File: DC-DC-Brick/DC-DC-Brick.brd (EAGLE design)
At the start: 50.8 x 76.2 mm, 20 parts

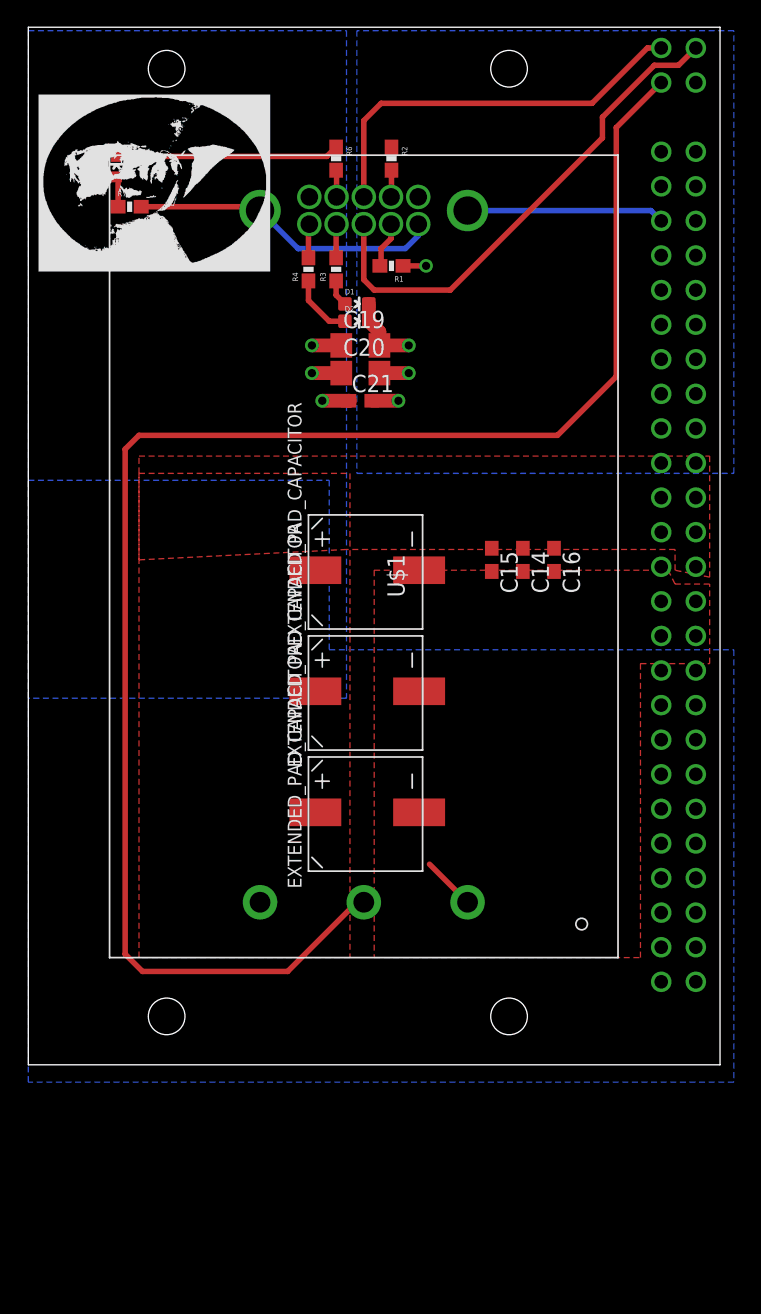
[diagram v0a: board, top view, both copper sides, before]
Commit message: FIxed connection issue
Gnd not connected in J purdue eye LED - fixed
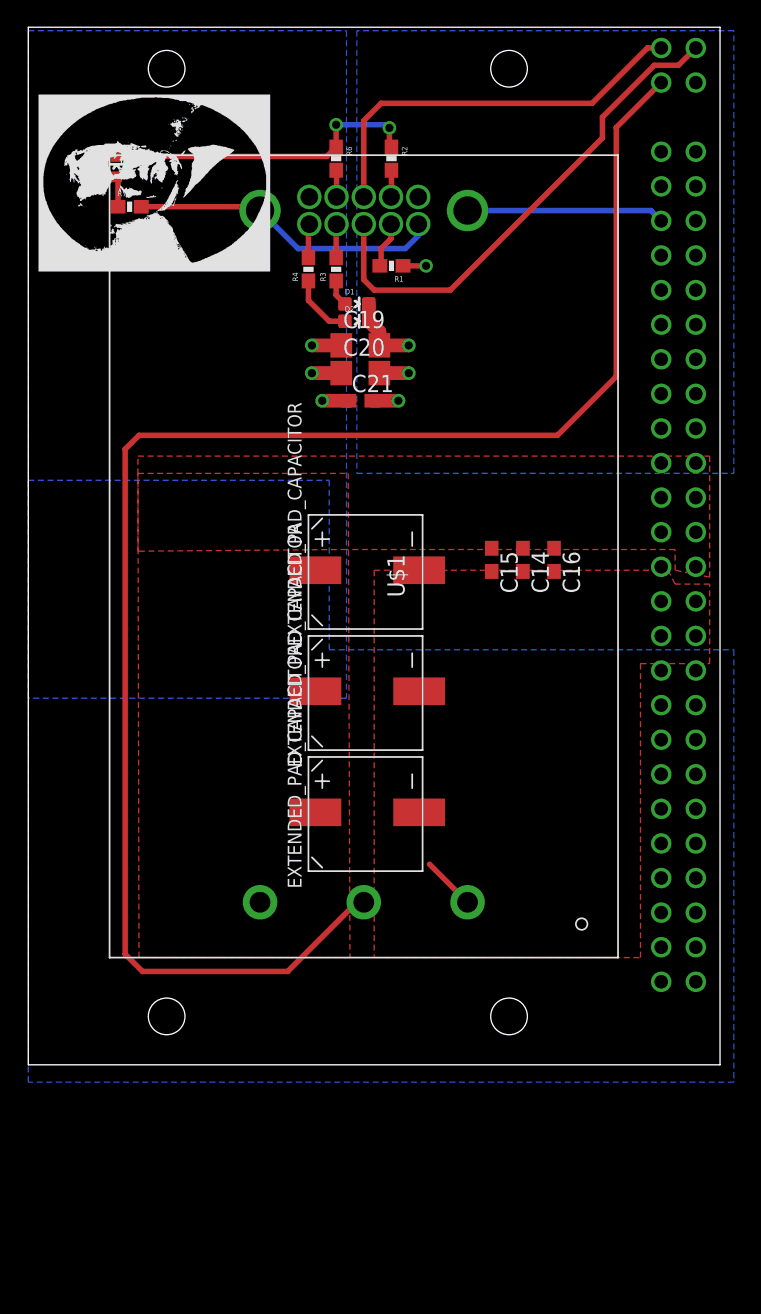
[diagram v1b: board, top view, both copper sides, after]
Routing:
- net GND: track 42.3 -> 49.4 mm, vias 4 -> 6
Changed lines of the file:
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@@
 <wire x1="6.477" y1="66.7138" x2="21.9218" y2="66.7138" width="0.4064" layer="1"/>
 <wire x1="21.9218" y1="66.7138" x2="22.606" y2="67.398" width="0.4064" layer="1"/>
-<wire x1="22.606" y1="67.398" x2="26.67" y2="67.398" width="0" layer="19" extent="1-1"/>
-<wire x1="28.638" y1="63.738" x2="26.67" y2="67.398" width="0" layer="19" extent="1-1"/>
+<wire x1="22.606" y1="67.398" x2="22.606" y2="69.0372" width="0.4064" layer="1"/>
+<via x="22.606" y="69.0372" extent="1-16" drill="0.6"/>
+<wire x1="22.606" y1="69.0372" x2="26.289" y2="69.0372" width="0.4064" layer="16"/>
+<wire x1="26.289" y1="69.0372" x2="26.5176" y2="68.8086" width="0.4064" layer="16"/>
+<via x="26.5176" y="68.8086" extent="1-16" drill="0.6"/>
+<wire x1="26.5176" y1="68.8086" x2="26.5176" y2="67.5504" width="0.4064" layer="1"/>
+<wire x1="26.5176" y1="67.5504" x2="26.67" y2="67.398" width="0.4064" layer="1"/>
 </signal>
 <signal name="N$6">
@@
 <contactref element="U$3" pad="P$29"/>
 <polygon width="0.4064" layer="1">
-<vertex x="8.128" y="44.704"/>
+<vertex x="8.0518" y="44.704"/>
 <vertex x="50.038" y="44.704"/>
 <vertex x="50.038" y="35.814"/>
@@
 <vertex x="47.498" y="37.846"/>
 <vertex x="23.368" y="37.846"/>
-<vertex x="8.128" y="37.084"/>
+<vertex x="8.0518" y="37.719"/>
 </polygon>
 <polygon width="0.4064" layer="1">
-<vertex x="8.128" y="43.434"/>
-<vertex x="23.622" y="43.434"/>
+<vertex x="8.0518" y="43.434"/>
+<vertex x="23.495" y="43.434"/>
 <vertex x="23.622" y="7.874"/>
 <vertex x="8.128" y="7.874"/>

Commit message: Changes made to DC bricks (see Google Doc)
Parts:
- removed C16: .1uF, rcl:C0603
- removed C19, C20: 15uF, rcl:C3216
- removed C21: 10uF, rcl:C0603
- removed C22V1, C22V5, C22V6: EXTENDED_PAD_CAPACITOR, ExtendedPadCap:MODIFIED-NICHICON-UX-8X10
- added C1: 1uF, rcl:C0603
- added C2: 10uF, rcl:C0603
- added C3, C4: 220uF, SparkFun-Capacitors:1206
- C15: value .1uF -> 10uF
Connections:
- net GND: now also C1.2, C2.2; no longer C19.2, C20.2, C21.2, D1.C
- net N$4: now also D1.C; no longer D1.A
- net V+: now also C1.1, C2.1, D1.A; no longer C19.1, C20.1, C21.1
- net V-: now also C3.2, C4.2; no longer C16.2, C22V1.P$1, C22V5.P$1, C22V6.P$1
- net VCC: now also C3.1, C4.1; no longer C16.1, C22V1.P$3, C22V5.P$3, C22V6.P$3
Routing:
- net GND: track 49.4 -> 40.9 mm, vias 6 -> 3
- net V+: track 29.4 -> 23.0 mm, vias 3 -> 0
- net N$4: track 1.96 -> 0.00 mm
